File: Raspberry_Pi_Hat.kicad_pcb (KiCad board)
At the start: 2 copper layers, 27.7 x 19.8 mm, 9 parts, among them J1 Raspberry_Pi_2_3, SW1 SW_DPST, U1 DHT22

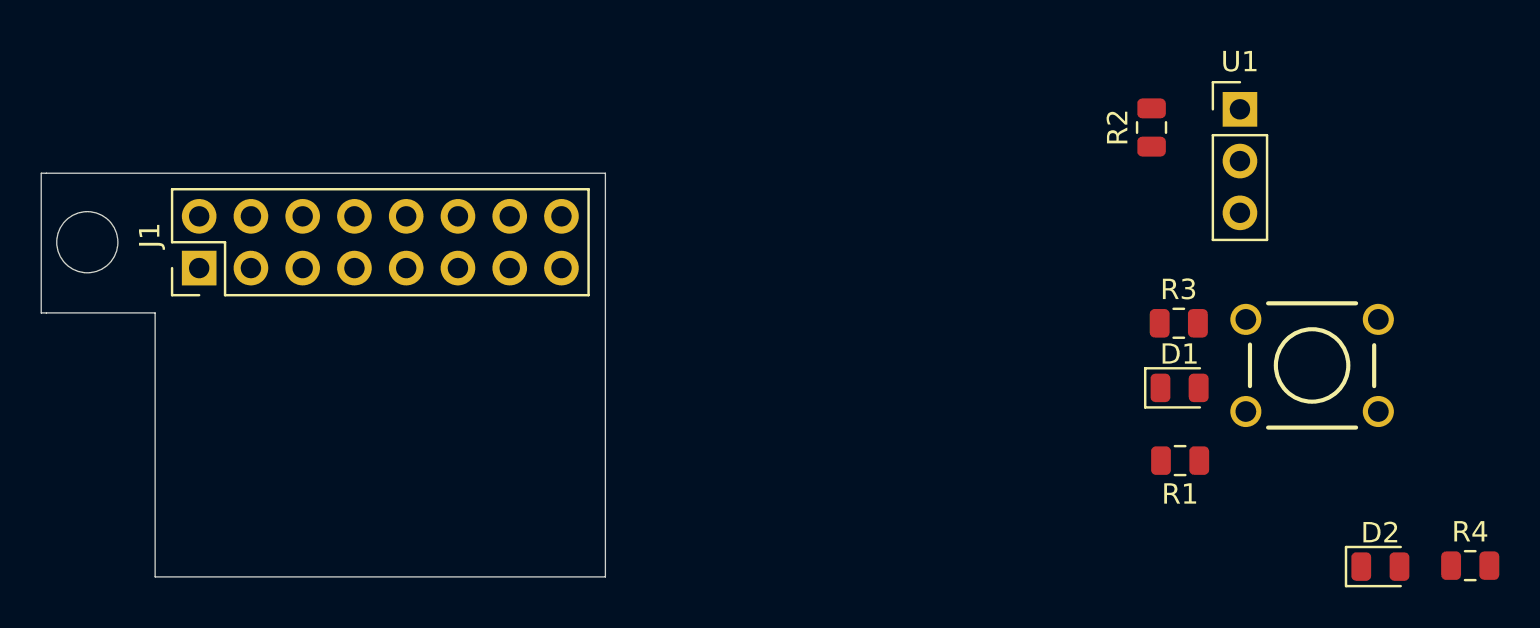
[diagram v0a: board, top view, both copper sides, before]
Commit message: routes board, gerber files and BOM
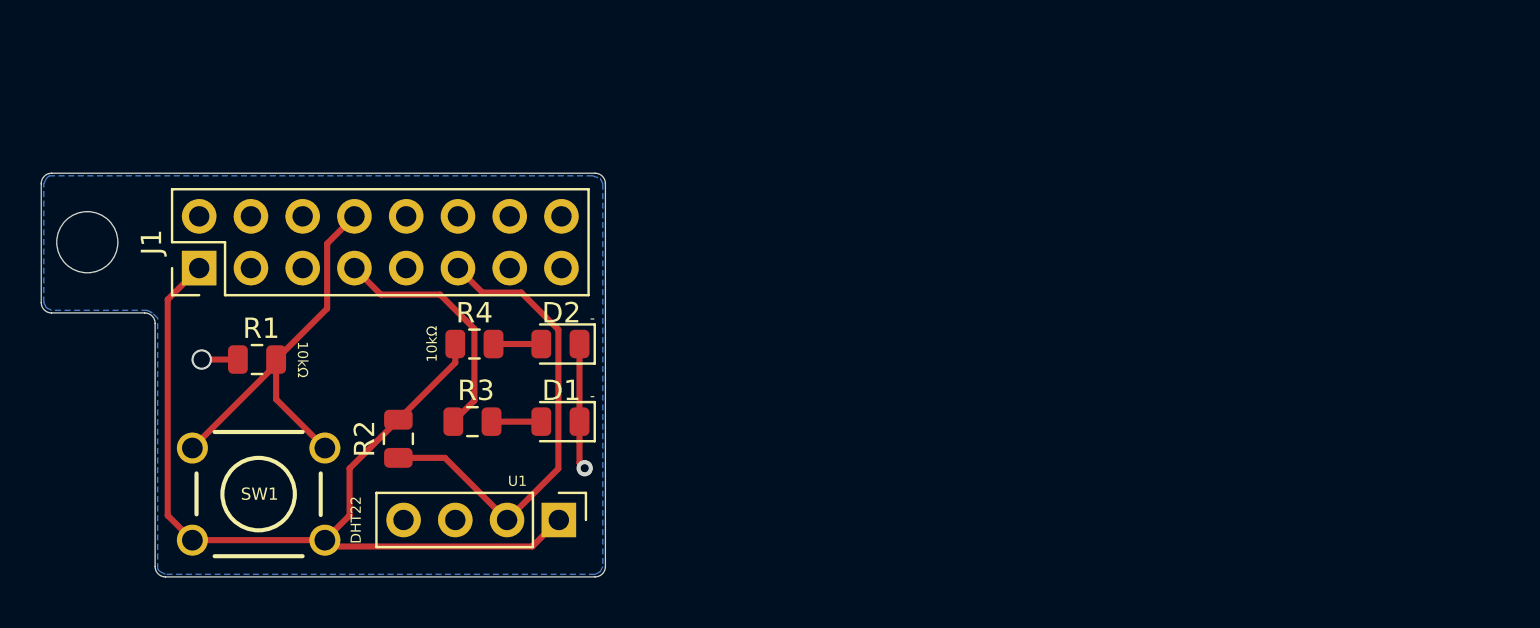
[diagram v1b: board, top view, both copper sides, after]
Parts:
- R1, R4: value R -> 10kΩ
- R2, R3: value R -> 330Ω
- U1: footprint Connector_PinHeader_2.54mm:PinHeader_1x03_P2.54mm_Vertical -> Connector_PinHeader_2.54mm:PinHeader_1x04_P2.54mm_Vertical
- moved SW1 52.1 mm to (116.1, 117.6), turned to 180 degrees
- moved R4 50.1 mm to (126.7, 110.2)
- moved R1 45.6 mm to (116.0, 111.0)
- moved D2 41.7 mm to (130.9, 110.2), turned to 180 degrees
- moved R2 40.0 mm to (122.9, 114.9)
- moved U1 39.0 mm to (130.8, 118.9), turned to 270 degrees
- moved R3 35.0 mm to (126.6, 114.0)
- moved D1 30.4 mm to (130.9, 114.0), turned to 180 degrees
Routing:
- net /3v3: track 0.00 -> 45.9 mm
- net Net-(J1-Pad11): track 0.00 -> 23.2 mm
- net /button_input: track 0.00 -> 20.0 mm
- net Net-(J1-Pad7): track 0.00 -> 12.1 mm
- net GND: track 0.00 -> 7.98 mm, vias 0 -> 2
- net Net-(D1-Pad2): track 0.00 -> 2.44 mm
- net Net-(D2-Pad2): track 0.00 -> 2.35 mm
- added copper zone on B.Cu, net GND
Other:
- outline, holes or cut-outs redrawn
- board text added: "-"
- board text added: "10kΩ"
